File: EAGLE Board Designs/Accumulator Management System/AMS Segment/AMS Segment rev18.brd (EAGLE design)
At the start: 275.2 x 86 mm, 347 parts, among them J1 CONNECTOR-2_MICROFIT_SMD_RIGH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, J10 CONNECTOR-2_MICROFIT_SMD_RIGH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, J100 CONNECTOR-1_5222_, J101 CONNECTOR-1_5222_, J102 CONNECTOR-1_5222_, J103 CONNECTOR-1_5222_, J104 CONNECTOR-1_5222_, J105 CONNECTOR-1_5222_, J106 CONNECTOR-1_5222_, J107 CONNECTOR-1_5222_, J108 CONNECTOR-1_5222_, J109 CONNECTOR-1_5222_, J110 CONNECTOR-1_5222_, J111 CONNECTOR-1_5222_, J112 CONNECTOR-1_5222_, J113 CONNECTOR-1_5222_, J114 CONNECTOR-1_5222_, J115 CONNECTOR-1_5222_, J116 CONNECTOR-1_5222_, J117 CONNECTOR-1_5222_, J118 CONNECTOR-1_5222_, J119 CONNECTOR-1_5222_, J120 CONNECTOR-1_5222_, J121 CONNECTOR-1_5222_, J2 CONNECTOR-2_MICROFIT_SMD_RIGH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, J3 CONNECTOR-2_MICROFIT_SMD_RIGH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, J4 CONNECTOR-2_MICROFIT_SMD_RIGH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, J5 CONNECTOR-2_MICROFIT_SMD_RIGH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, J6 CONNECTOR-2_MICROFIT_SMD_RIGH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, J7 CONNECTOR-2_MICROFIT_SMD_RIGH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, J8 CONNECTOR-2_MICROFIT_SMD_RIGH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, J9 CONNECTOR-2_MICROFIT_SMD_RIGH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, T1 TRANSFORMER_HM2112ZNLT, U1 SHT31-ARP-B, U2 LTC6811-2, U3 LT3990-5, U4 LT3990-5, U5 LTC6811-2, U6 SHT31-ARP-B

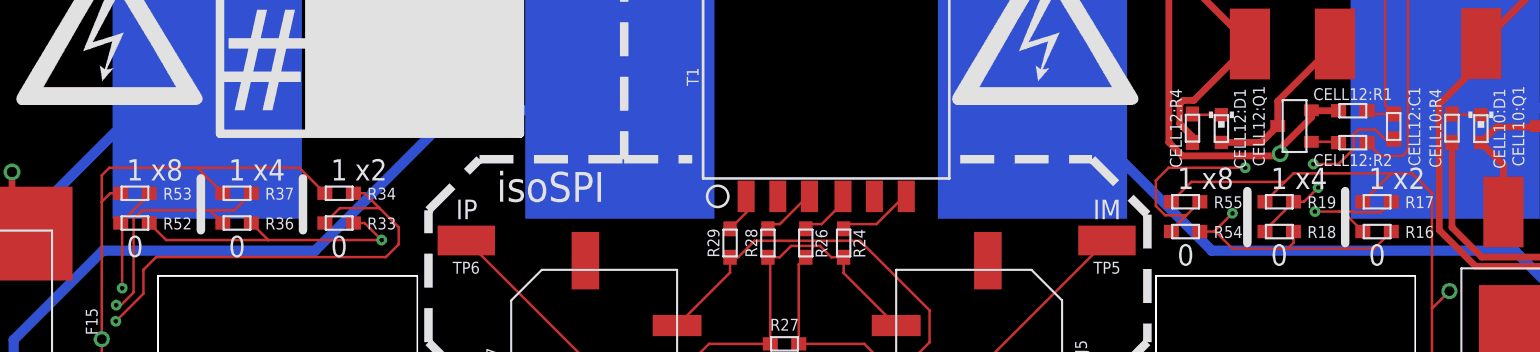
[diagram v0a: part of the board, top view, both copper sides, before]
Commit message: moved text around
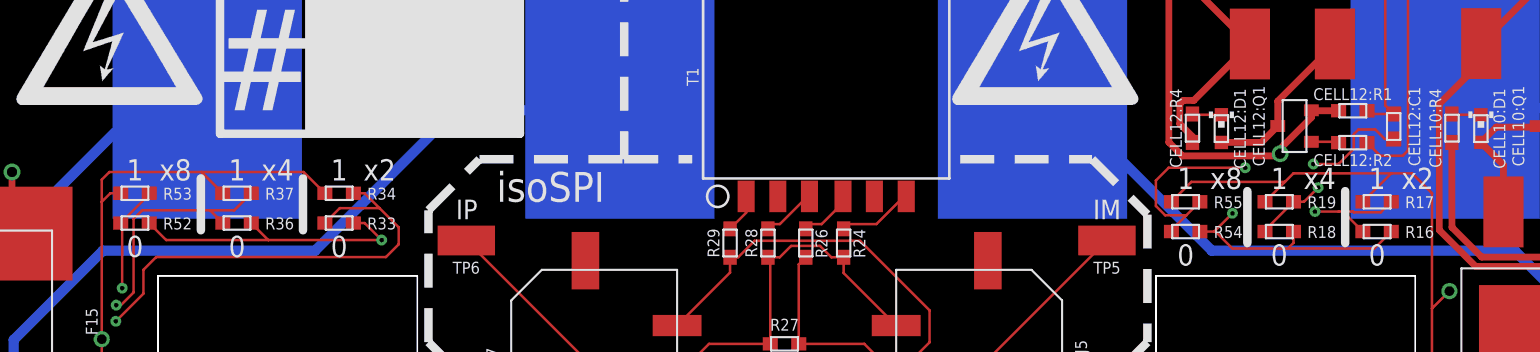
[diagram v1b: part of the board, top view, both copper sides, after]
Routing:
- net VREGU: track 306.8 -> 306.1 mm
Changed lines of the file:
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@@
 <text x="110.236" y="-67.564" size="1.27" layer="21" font="vector" align="bottom-center">1</text>
 <text x="104.14" y="-67.564" size="1.27" layer="21" font="vector" align="bottom-center">1</text>
-<text x="112.141" y="-67.564" size="1.27" layer="21" font="vector" align="bottom-center">x2</text>
-<text x="106.045" y="-67.564" size="1.27" layer="21" font="vector" align="bottom-center">x4</text>
-<text x="174.117" y="-68.072" size="1.27" layer="21" font="vector" align="bottom-center">x2</text>
-<text x="168.275" y="-68.072" size="1.27" layer="21" font="vector" align="bottom-center">x4</text>
+<text x="112.649" y="-67.564" size="1.27" layer="21" font="vector" align="bottom-center">x2</text>
+<text x="106.553" y="-67.564" size="1.27" layer="21" font="vector" align="bottom-center">x4</text>
+<text x="174.625" y="-68.072" size="1.27" layer="21" font="vector" align="bottom-center">x2</text>
+<text x="168.783" y="-68.072" size="1.27" layer="21" font="vector" align="bottom-center">x4</text>
 <wire x1="121.6865125" y1="-34.5645125" x2="118.491" y2="-31.369" width="0.508" layer="22" style="shortdash"/>
 <wire x1="127.254" y1="-40.132" x2="125.4554875" y2="-38.3334875" width="0.508" layer="22" style="shortdash"/>
@@
 <wire x1="155.194" y1="-66.294" x2="158.496" y2="-69.596" width="0.508" layer="21" style="shortdash"/>
 <text x="98.044" y="-67.564" size="1.27" layer="21" font="vector" align="bottom-center">1</text>
-<text x="99.949" y="-67.564" size="1.27" layer="21" font="vector" align="bottom-center">x8</text>
+<text x="100.457" y="-67.564" size="1.27" layer="21" font="vector" align="bottom-center">x8</text>
 <wire x1="101.981" y1="-70.5358" x2="101.981" y2="-67.437" width="0.508" layer="21"/>
 <text x="98.044" y="-72.136" size="1.27" layer="21" font="vector" align="bottom-center">0</text>
@@
 <text x="160.782" y="-72.644" size="1.27" layer="21" font="vector" align="bottom-center">0</text>
 <text x="160.782" y="-68.072" size="1.27" layer="21" font="vector" align="bottom-center">1</text>
-<text x="162.687" y="-68.072" size="1.27" layer="21" font="vector" align="bottom-center">x8</text>
+<text x="163.195" y="-68.072" size="1.27" layer="21" font="vector" align="bottom-center">x8</text>
 </plain>
 <attributes>
@@
 <wire x1="52.9264" y1="-31.9221" x2="64.5031" y2="-20.3454" width="0.381" layer="15"/>
 <contactref element="R53" pad="1"/>
-<wire x1="96.52" y1="-66.802" x2="101.766" y2="-66.802" width="0.1524" layer="1"/>
-<wire x1="101.766" y1="-66.802" x2="103.29" y2="-68.326" width="0.1524" layer="1"/>
-<wire x1="101.766" y1="-66.802" x2="107.862" y2="-66.802" width="0.1524" layer="1"/>
-<wire x1="107.862" y1="-66.802" x2="109.386" y2="-68.326" width="0.1524" layer="1"/>
+<wire x1="96.52" y1="-67.056" x2="102.02" y2="-67.056" width="0.1524" layer="1"/>
+<wire x1="102.02" y1="-67.056" x2="103.29" y2="-68.326" width="0.1524" layer="1"/>
+<wire x1="102.02" y1="-67.056" x2="108.116" y2="-67.056" width="0.1524" layer="1"/>
+<wire x1="108.116" y1="-67.056" x2="109.386" y2="-68.326" width="0.1524" layer="1"/>
 <wire x1="96.0628" y1="-77.0382" x2="96.0628" y2="-68.834" width="0.1524" layer="1"/>
-<wire x1="96.0628" y1="-68.834" x2="96.0628" y2="-67.2592" width="0.1524" layer="1"/>
-<wire x1="96.0628" y1="-67.2592" x2="96.52" y2="-66.802" width="0.1524" layer="1"/>
+<wire x1="96.0628" y1="-68.834" x2="96.0628" y2="-67.5132" width="0.1524" layer="1"/>
+<wire x1="96.0628" y1="-67.5132" x2="96.52" y2="-67.056" width="0.1524" layer="1"/>
 <wire x1="96.0628" y1="-68.834" x2="96.5708" y2="-68.326" width="0.1524" layer="1"/>
 <wire x1="96.5708" y1="-68.326" x2="97.194" y2="-68.326" width="0.1524" layer="1"/>

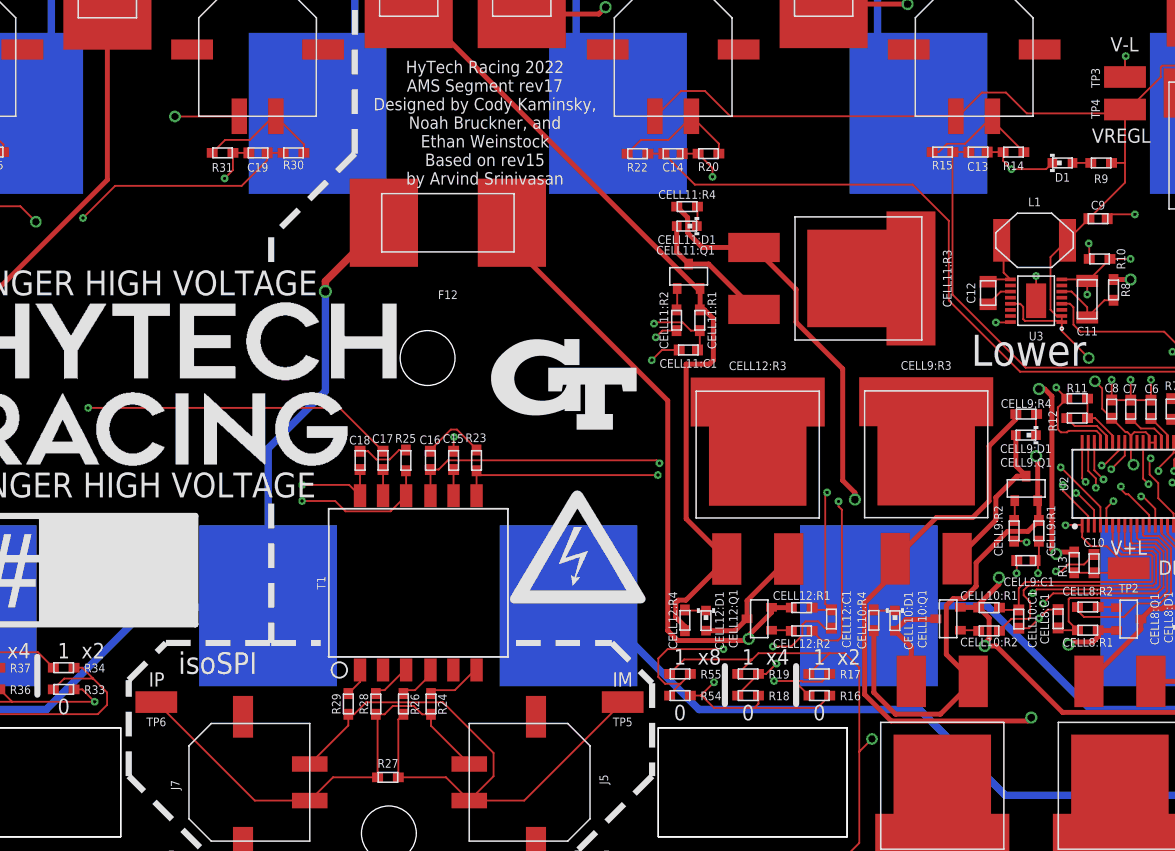
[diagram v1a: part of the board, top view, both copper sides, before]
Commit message: fixed isospi transformer
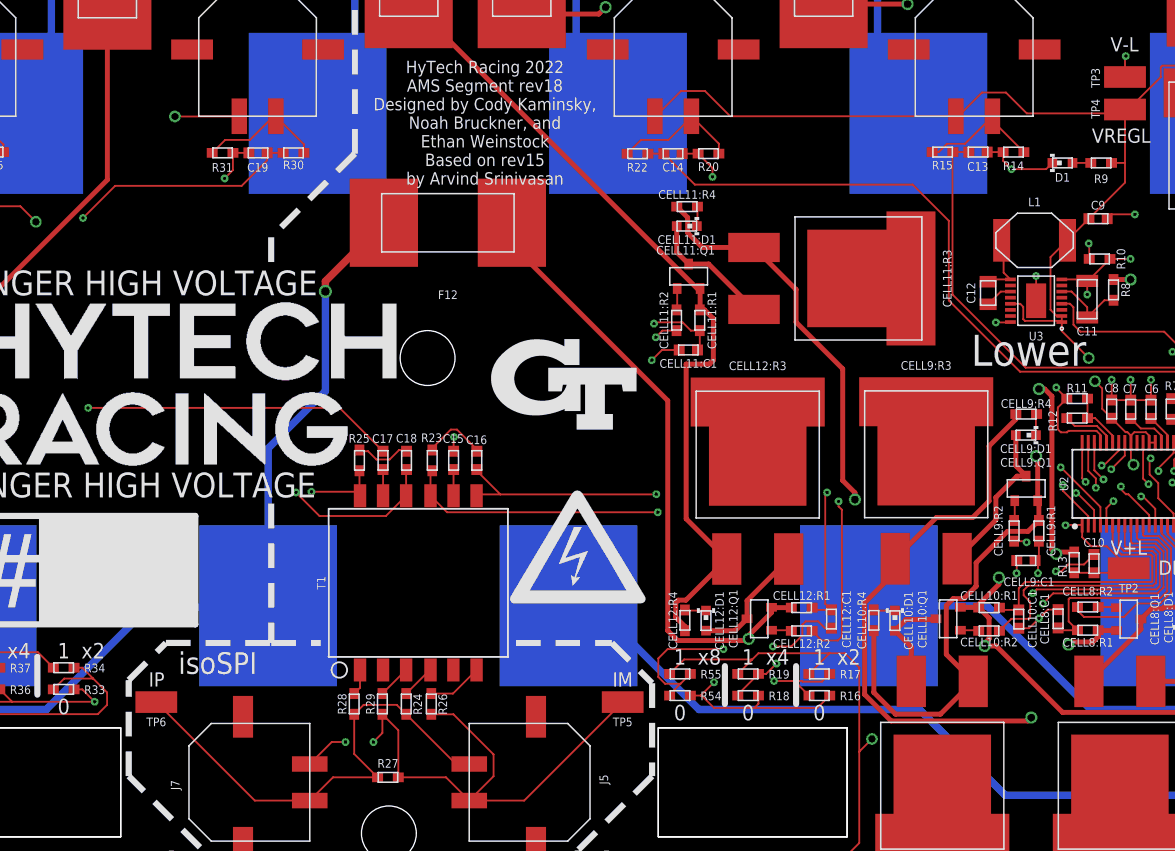
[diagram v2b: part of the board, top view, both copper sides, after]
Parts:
- moved C16 3.81 mm to (144.1, -51.3)
- moved C18 3.81 mm to (138.4, -51.3)
- moved R25 3.81 mm to (134.5, -51.3)
- moved R23 3.63 mm to (140.5, -51.3)
- moved R29 2.79 mm to (136.4, -71.3)
- moved R26 2.29 mm to (140.4, -71.3)
- moved R24 2.03 mm to (138.3, -71.3)
- moved R28 1.78 mm to (134.1, -71.3)
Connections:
- net IML: now also T1.7; no longer T1.9
- net IMU: now also T1.10; no longer T1.12
- net IPL: now also T1.9; no longer T1.7
- net IPU: now also T1.12; no longer T1.10
- net N$22: now also T1.3; no longer T1.1
- net N$27: now also T1.1; no longer T1.3
- net N$32: now also T1.6; no longer T1.4
- net N$33: now also T1.4; no longer T1.6
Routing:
- net IPL: track 56.6 -> 62.1 mm
- net IMU: track 62.4 -> 67.1 mm
- net IPU: track 65.6 -> 61.4 mm
- net IM: track 52.0 -> 47.9 mm, vias 0 -> 2
- net IML: track 62.7 -> 59.5 mm
- net IP: track 38.0 -> 40.0 mm
- net N$33: track 4.54 -> 2.79 mm
- net N$32: track 3.25 -> 4.51 mm
- net N$27: track 3.28 -> 2.13 mm
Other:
- board text added: "HyTech Racing 2022 AMS Segment rev18 Designed by Cody Kaminsky, Noah Bruckner, and Ethan Weinstock Based on rev15 by Arvind Srinivasan"
- board text removed: "HyTech Racing 2022 AMS Segment rev17 Designed by Cody Kaminsky, Noah Bruckner, and Ethan Weinstock Based on rev15 by Arvind Srinivasan"

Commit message: passed review
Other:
- board text added: "HyTech Racing 2022 AMS Segment rev18 Designed by Liwei Sun Based on AMS Segment rev17 By Cody Kaminsky"
- board text removed: "HyTech Racing 2022 AMS Segment rev18 Designed by Cody Kaminsky, Noah Bruckner, and Ethan Weinstock Based on rev15 by Arvind Srinivasan"
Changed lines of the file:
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@@
 <text x="144.78" y="-23.622" size="1.016" layer="21" font="vector" align="center">HyTech Racing 2022
 AMS Segment rev18
-Designed by Cody Kaminsky,
-Noah Bruckner, and
-Ethan Weinstock
-Based on rev15
-by Arvind Srinivasan
+Designed by Liwei Sun
+Based on AMS Segment rev17
+By Cody Kaminsky
 </text>
 <text x="156.083" y="-69.8754" size="1.1684" layer="21" font="vector" align="bottom-center">IM</text>
